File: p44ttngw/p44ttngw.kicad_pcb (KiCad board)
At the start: 2 copper layers, 90.5 x 56 mm, 67 parts, among them J1 CONN_02X04, J2 HLJ-6115ANL, J3 CONN_02X12, J4 USB_A, J6 USB_Micro_AB, J8 HLJ-6115ANL, P1 FDI_Cable, P3 CONN_02X02, SW1 Omron PB, U1 ONION-OMEGA2S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

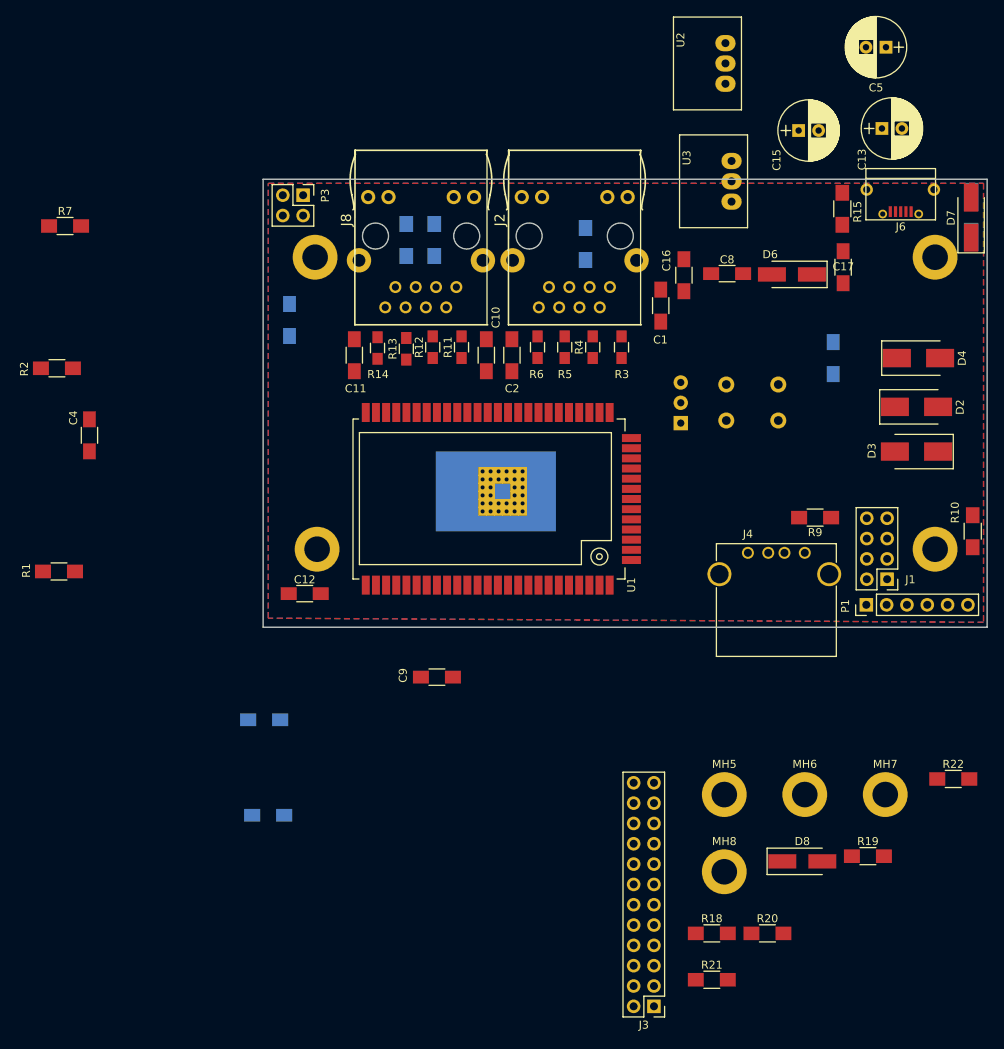
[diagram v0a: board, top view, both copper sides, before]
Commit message: Complete PCB for P44-DSB Hammond case, but mechanical check pending
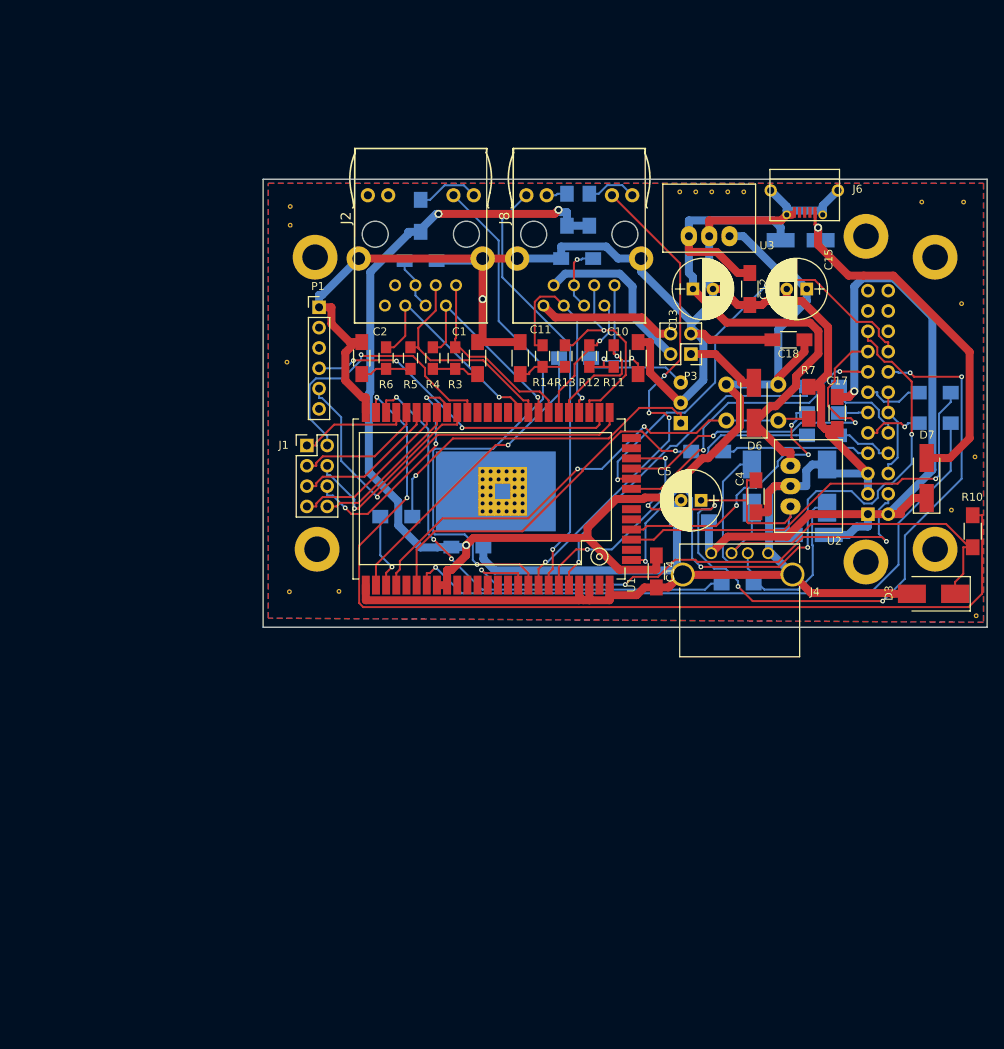
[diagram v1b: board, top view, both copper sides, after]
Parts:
- removed C19: 100nF, Capacitors_SMD:C_1206_HandSoldering
- removed MH5, MH6, MH7, MH8: CONN_01X01, Mounting_Holes:MountingHole_3.2mm_M3_DIN965_Pad
- added VIA: Stitching-VIA-0.6mm, plan44:Stitching-VIA-0.6mm, F.Cu at (124.1, 65.6)
- added VIA: Stitching-VIA-0.6mm, plan44:Stitching-VIA-0.6mm, F.Cu at (158.0, 105.4)
- added VIA: Stitching-VIA-0.6mm, plan44:Stitching-VIA-0.6mm, F.Cu at (161.1, 118.6)
- added VIA: Stitching-VIA-0.6mm, plan44:Stitching-VIA-0.6mm, F.Cu at (81.5, 115.5)
- added VIA: Stitching-VIA-0.6mm, plan44:Stitching-VIA-0.6mm, F.Cu at (75.3, 115.6)
- added VIA: Stitching-VIA-0.6mm, plan44:Stitching-VIA-0.6mm, F.Cu at (75.0, 86.9)
- added VIA: Stitching-VIA-0.6mm, plan44:Stitching-VIA-0.6mm, F.Cu at (75.4, 69.7)
- added VIA: Stitching-VIA-0.6mm, plan44:Stitching-VIA-0.6mm, F.Cu at (75.4, 67.4)
- added VIA: Stitching-VIA-0.6mm, plan44:Stitching-VIA-0.6mm, F.Cu at (126.1, 65.6)
- added VIA: Stitching-VIA-0.6mm, plan44:Stitching-VIA-0.6mm, F.Cu at (128.1, 65.6)
- added VIA: Stitching-VIA-0.6mm, plan44:Stitching-VIA-0.6mm, F.Cu at (130.1, 65.6)
- added VIA: Stitching-VIA-0.6mm, plan44:Stitching-VIA-0.6mm, F.Cu at (132.1, 65.6)
- added VIA: Stitching-VIA-0.6mm, plan44:Stitching-VIA-0.6mm, F.Cu at (154.3, 66.9)
- added VIA: Stitching-VIA-0.6mm, plan44:Stitching-VIA-0.6mm, F.Cu at (159.6, 66.9)
- added VIA: Stitching-VIA-0.6mm, plan44:Stitching-VIA-0.6mm, F.Cu at (159.3, 79.6)
- added VIA: Stitching-VIA-0.6mm, plan44:Stitching-VIA-0.6mm, F.Cu at (161.0, 98.7)
- C14, C18: moved to F.Cu
- C16, C8, C9, D2, D4, D8, R1, R15, R18, R19, R2, R20, R21, R22, R9: moved to B.Cu
- J3: value CONN_02X12 -> RAK831; footprint Pin_Headers:Pin_Header_Straight_2x12_Pitch2.54mm -> RAK831; moved to B.Cu
- moved R7 95.6 mm to (140.2, 91.9), turned to 270 degrees
- moved C4 83.7 mm to (133.6, 103.6)
- moved C18 80.9 mm to (137.7, 84.1), turned to 180 degrees
- moved P1 77.9 mm to (79.0, 80.0), turned to 0 degrees
- moved J1 74.4 mm to (77.5, 97.3), turned to 0 degrees
- moved R21 72.2 mm to (142.0, 93.2), turned to 180 degrees
- moved R1 69.8 mm to (111.0, 86.4), turned to 0 degrees
- moved R20 68.7 mm to (142.0, 89.9)
- moved C12 67.4 mm to (132.8, 77.7), turned to 270 degrees
- moved R18 63.8 mm to (142.0, 96.0)
- moved C5 61.2 mm to (126.7, 104.1)
- moved J3 61.1 mm to (147.3, 112.3)
- moved U2 58.5 mm to (137.9, 104.9), turned to 90 degrees
- moved C14 57.3 mm to (121.2, 113.0), turned to 270 degrees
- moved C3 56.3 mm to (125.7, 106.7), turned to 180 degrees
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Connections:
- net Net-(C4-Pad1) renamed /5VPWR
- C17 pad 1: +3V3 -> +5V
- C3 pad 1: +3V3 -> +5V
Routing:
- net GND: track 0.00 -> 363.1 mm, vias 0 -> 1
- net +3V3: track 0.00 -> 181.8 mm, vias 0 -> 3
- net /USB-: track 0.00 -> 121.5 mm, vias 0 -> 2
- net +5V: track 0.00 -> 95.8 mm, vias 0 -> 1
- net /SPI_MOSI: track 0.00 -> 94.7 mm, vias 0 -> 7
- net /RADIO_EN_B: track 0.00 -> 84.0 mm, vias 0 -> 1
- net /RAK_RESET: track 0.00 -> 80.0 mm, vias 0 -> 4
- net +24V: track 0.00 -> 73.8 mm
- net /ETH1_LED: track 0.00 -> 73.6 mm, vias 0 -> 1
- net /LNA_EN_A: track 0.00 -> 67.6 mm, vias 0 -> 3
- net /ETH0_LED: track 0.00 -> 63.0 mm, vias 0 -> 4
- net Net-(R7-Pad2): track 0.00 -> 62.3 mm, vias 0 -> 2
- net /USB+: track 0.00 -> 61.7 mm, vias 0 -> 3
- net /SPI_CLK: track 0.00 -> 55.5 mm, vias 0 -> 2
- net /WLAN_LED: track 0.00 -> 54.6 mm, vias 0 -> 1
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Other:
- net class PowerSmall: clearance 0.15 -> 0.1

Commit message: Completely redesigned for IP65 Hammond 1554E (90x90x60)
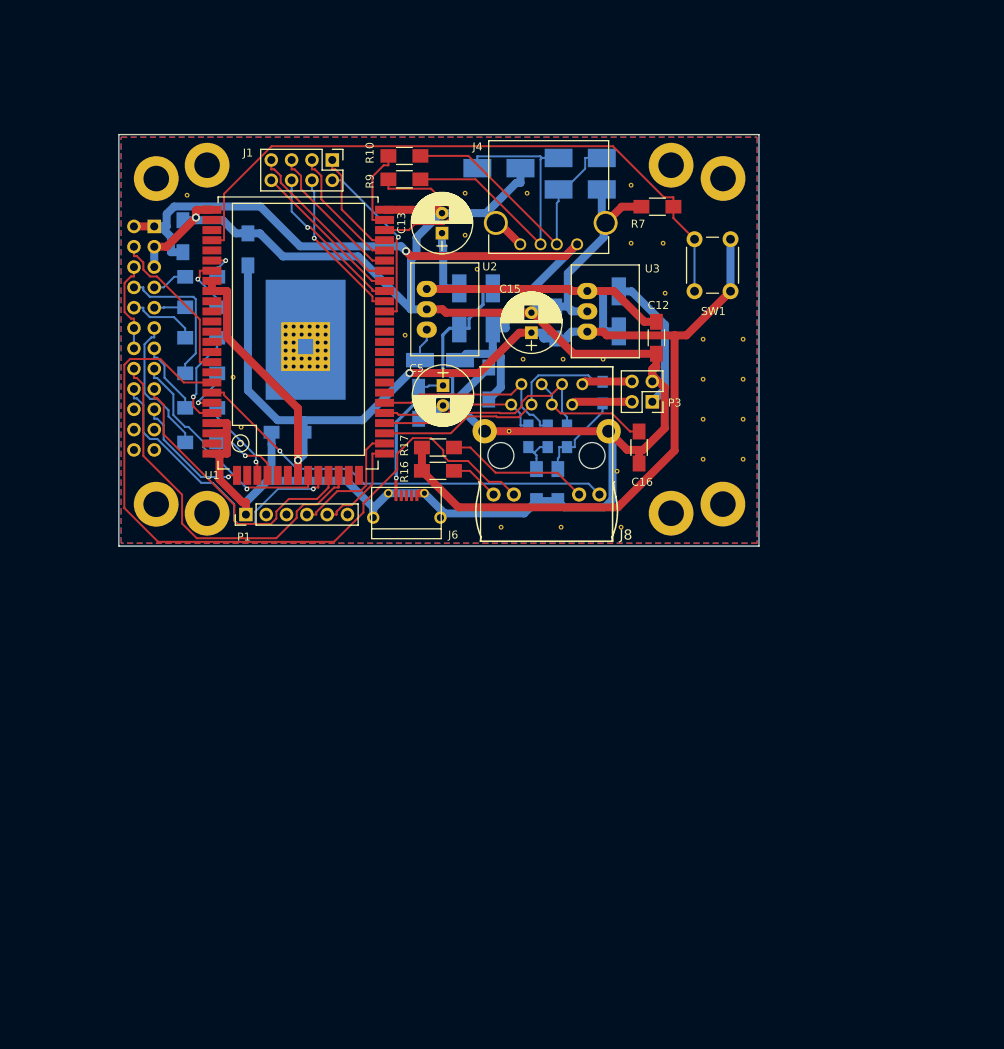
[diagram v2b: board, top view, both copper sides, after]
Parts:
- removed C1, C2: 100nF, Capacitors_SMD:C_1206_HandSoldering
- removed C8: 1uF, Capacitors_SMD:C_1206_HandSoldering
- removed D1: Everlight 339-1SURSYGW/S530-A3, LEDs:LED_D5.0mm-3
- removed J2: HLJ-6115ANL, plan44:HLJ-6115ANL
- removed R1: 470, Resistors_SMD:R_1206_HandSoldering
- removed R2: 1k2, Resistors_SMD:R_1206_HandSoldering
- removed R3, R4, R5, R6: 49.9_1%, Resistors_SMD:R_0805_HandSoldering
- removed R8: 1k, Resistors_SMD:R_1206_HandSoldering
- removed the VIA at (124.1, 65.6)
- removed the VIA at (158.0, 105.4)
- removed the VIA at (161.1, 118.6)
- removed the VIA at (81.5, 115.5)
- removed the VIA at (75.3, 115.6)
- removed the VIA at (75.0, 86.9)
- removed the VIA at (75.4, 69.7)
- removed the VIA at (75.4, 67.4)
- removed the VIA at (126.1, 65.6)
- removed the VIA at (128.1, 65.6)
- removed the VIA at (130.1, 65.6)
- removed the VIA at (132.1, 65.6)
- removed the VIA at (154.3, 66.9)
- removed the VIA at (159.6, 66.9)
- removed the VIA at (159.3, 79.6)
- removed the VIA at (161.0, 98.7)
- added VIA: Stitching-VIA-0.6mm, plan44:Stitching-VIA-0.6mm, F.Cu at (69.2, 95.0)
- added VIA: Stitching-VIA-0.6mm, plan44:Stitching-VIA-0.6mm, F.Cu at (118.0, 72.0)
- added VIA: Stitching-VIA-0.6mm, plan44:Stitching-VIA-0.6mm, F.Cu at (118.0, 64.8)
- added VIA: Stitching-VIA-0.6mm, plan44:Stitching-VIA-0.6mm, F.Cu at (105.0, 65.8)
- added VIA: Stitching-VIA-0.6mm, plan44:Stitching-VIA-0.6mm, F.Cu at (114.5, 86.5)
- added VIA: Stitching-VIA-0.6mm, plan44:Stitching-VIA-0.6mm, F.Cu at (109.5, 86.5)
- added VIA: Stitching-VIA-0.6mm, plan44:Stitching-VIA-0.6mm, F.Cu at (104.5, 86.5)
- added VIA: Stitching-VIA-0.6mm, plan44:Stitching-VIA-0.6mm, F.Cu at (132.0, 84.0)
- added VIA: Stitching-VIA-0.6mm, plan44:Stitching-VIA-0.6mm, F.Cu at (127.0, 84.0)
- added VIA: Stitching-VIA-0.6mm, plan44:Stitching-VIA-0.6mm, F.Cu at (132.0, 89.0)
- added VIA: Stitching-VIA-0.6mm, plan44:Stitching-VIA-0.6mm, F.Cu at (127.0, 89.0)
- added VIA: Stitching-VIA-0.6mm, plan44:Stitching-VIA-0.6mm, F.Cu at (116.2, 100.5)
- added VIA: Stitching-VIA-0.6mm, plan44:Stitching-VIA-0.6mm, F.Cu at (132.0, 94.0)
- added VIA: Stitching-VIA-0.6mm, plan44:Stitching-VIA-0.6mm, F.Cu at (127.0, 94.0)
- added VIA: Stitching-VIA-0.6mm, plan44:Stitching-VIA-0.6mm, F.Cu at (132.0, 99.0)
- added VIA: Stitching-VIA-0.6mm, plan44:Stitching-VIA-0.6mm, F.Cu at (127.0, 99.0)
- added VIA: Stitching-VIA-0.6mm, plan44:Stitching-VIA-0.6mm, F.Cu at (116.8, 107.5)
- added VIA: Stitching-VIA-0.6mm, plan44:Stitching-VIA-0.6mm, F.Cu at (109.2, 107.5)
- added VIA: Stitching-VIA-0.6mm, plan44:Stitching-VIA-0.6mm, F.Cu at (101.8, 107.5)
- added VIA: Stitching-VIA-0.6mm, plan44:Stitching-VIA-0.6mm, F.Cu at (68.2, 88.8)
- added VIA: Stitching-VIA-0.6mm, plan44:Stitching-VIA-0.6mm, F.Cu at (62.5, 66.0)
- added VIA: Stitching-VIA-0.6mm, plan44:Stitching-VIA-0.6mm, F.Cu at (102.8, 95.5)
- added VIA: Stitching-VIA-0.6mm, plan44:Stitching-VIA-0.6mm, F.Cu at (89.8, 83.5)
- added VIA: Stitching-VIA-0.6mm, plan44:Stitching-VIA-0.6mm, F.Cu at (98.8, 75.2)
- added VIA: Stitching-VIA-0.6mm, plan44:Stitching-VIA-0.6mm, F.Cu at (97.2, 71.0)
- added VIA: Stitching-VIA-0.6mm, plan44:Stitching-VIA-0.6mm, F.Cu at (97.2, 65.8)
- added VIA: Stitching-VIA-0.6mm, plan44:Stitching-VIA-0.6mm, F.Cu at (122.2, 78.2)
- added VIA: Stitching-VIA-0.6mm, plan44:Stitching-VIA-0.6mm, F.Cu at (122.0, 72.0)
- C10, C11, C14, C17, C18, C4, D3, D6, D7, R11, R12, R13, R14: moved to B.Cu
- C16, R16, R17, R9, SW1: moved to F.Cu
- J3: footprint RAK831 -> plan44:RAK831
- moved J3 101.2 mm to (58.7, 63.5), turned to 0 degrees
- moved R19 92.8 mm to (64.3, 80.0)
- moved R22 91.7 mm to (64.3, 92.6)
- moved R10 85.1 mm to (89.7, 61.1), turned to 0 degrees
- moved R18 78.1 mm to (64.3, 88.3), turned to 180 degrees
- moved R20 78.0 mm to (64.3, 83.8), turned to 180 degrees
- moved R21 77.8 mm to (64.3, 96.9), turned to 0 degrees
- moved C3 73.0 mm to (62.0, 71.1), turned to 90 degrees
- moved D3 67.1 mm to (111.6, 65.3), turned to 0 degrees
- moved R15 66.9 mm to (64.3, 76.2), turned to 0 degrees
- moved R9 65.5 mm to (89.7, 64.0)
- moved C14 65.0 mm to (70.1, 72.8), turned to 90 degrees
- moved J6 62.7 mm to (89.9, 104.9), turned to 0 degrees
- moved D7 58.2 mm to (100.7, 80.1)
- moved D4 57.1 mm to (101.5, 62.6), turned to 0 degrees
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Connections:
- U1 pad B10: /ETH1_RX- -> (no net)
- U1 pad B7: /ETH1_TX+ -> (no net)
- U1 pad B8: /ETH1_TX- -> (no net)
- U1 pad B9: /ETH1_RX+ -> (no net)
- U1 pad C23: Net-(R2-Pad1) -> (no net)
- U1 pad C24: Net-(R1-Pad1) -> (no net)
- U1 pad C9: /ETH1_LED -> (no net)
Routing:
- net /USB-: track 121.5 -> 10.7 mm, vias 2 -> 0
- net /RADIO_EN_B: track 84.0 -> 7.24 mm
- net /ETH1_LED: track 73.6 -> 0.00 mm, vias 1 -> 0
- net GND: track 363.1 -> 292.5 mm
- net /RAK_RESET: track 80.0 -> 15.7 mm, vias 4 -> 1
- net /SPI_MOSI: track 94.7 -> 47.0 mm, vias 7 -> 0
- net /LNA_EN_A: track 67.6 -> 20.1 mm, vias 3 -> 0
- net Net-(D1-Pad1): track 43.4 -> 0.00 mm, vias 1 -> 0
- net /RADIO_RST: track 52.7 -> 10.5 mm
- net /RADIO_EN_A: track 46.0 -> 4.32 mm
- net /USB+: track 61.7 -> 20.1 mm, vias 3 -> 0
- net Net-(R1-Pad1): track 38.8 -> 0.00 mm, vias 1 -> 0
- net /Omega_TX: track 51.3 -> 12.8 mm, vias 1 -> 0
- net /PA_G8: track 40.5 -> 6.37 mm
- net /PA_G16: track 43.5 -> 12.5 mm
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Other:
- board size 90.5 x 56 mm -> 80 x 51.4 mm

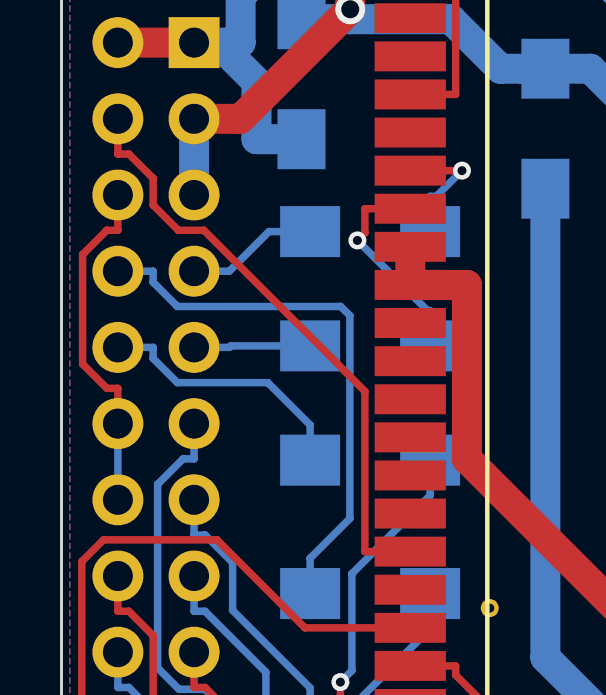
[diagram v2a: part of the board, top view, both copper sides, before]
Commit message: RAK831 pins 6,12 and 14 were connected together, but not to GND as they should. Fixed manually in layout, track width between 6 and 12 is narrow, no room for power net (and not needed).
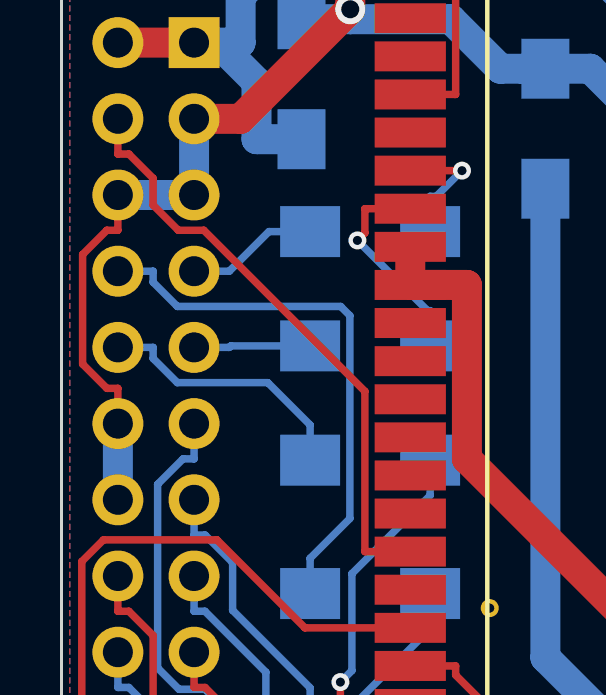
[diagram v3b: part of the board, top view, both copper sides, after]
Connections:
- J3 pad 12: Net-(J3-Pad12) -> GND
- J3 pad 14: Net-(J3-Pad12) -> GND
- J3 pad 20: (no net) -> Net-(J3-Pad20)
- J3 pad 21: (no net) -> Net-(J3-Pad21)
- J3 pad 22: (no net) -> Net-(J3-Pad22)
- J3 pad 23: (no net) -> Net-(J3-Pad23)
- J3 pad 24: (no net) -> Net-(J3-Pad24)
- J3 pad 6: Net-(J3-Pad12) -> GND
- J6 pad 2: (no net) -> Net-(J6-Pad2)
- J6 pad 3: (no net) -> Net-(J6-Pad3)
- J6 pad 4: (no net) -> Net-(J6-Pad4)
- MH1 pad 1: (no net) -> Net-(MH1-Pad1)
- MH2 pad 1: (no net) -> Net-(MH2-Pad1)
- MH3 pad 1: (no net) -> Net-(MH3-Pad1)
- MH4 pad 1: (no net) -> Net-(MH4-Pad1)
- P1 pad 2: (no net) -> Net-(P1-Pad2)
- P1 pad 3: (no net) -> Net-(P1-Pad3)
- P1 pad 6: (no net) -> Net-(P1-Pad6)
- U1 pad A12: (no net) -> Net-(U1-PadA12)
- U1 pad A13: (no net) -> Net-(U1-PadA13)
- U1 pad A2: (no net) -> Net-(U1-PadA2)
- U1 pad A5: (no net) -> Net-(U1-PadA5)
- U1 pad A6: (no net) -> Net-(U1-PadA6)
- U1 pad B10: (no net) -> Net-(U1-PadB10)
- U1 pad B11: (no net) -> Net-(U1-PadB11)
- U1 pad B12: (no net) -> Net-(U1-PadB12)
- U1 pad B13: (no net) -> Net-(U1-PadB13)
- U1 pad B14: (no net) -> Net-(U1-PadB14)
- U1 pad B7: (no net) -> Net-(U1-PadB7)
- U1 pad B8: (no net) -> Net-(U1-PadB8)
- U1 pad B9: (no net) -> Net-(U1-PadB9)
- U1 pad C11: (no net) -> Net-(U1-PadC11)
- U1 pad C12: (no net) -> Net-(U1-PadC12)
- U1 pad C13: (no net) -> Net-(U1-PadC13)
- U1 pad C14: (no net) -> Net-(U1-PadC14)
- U1 pad C15: (no net) -> Net-(U1-PadC15)
- U1 pad C16: (no net) -> Net-(U1-PadC16)
- U1 pad C2: (no net) -> Net-(U1-PadC2)
- U1 pad C21: (no net) -> Net-(U1-PadC21)
- U1 pad C23: (no net) -> Net-(U1-PadC23)
- U1 pad C24: (no net) -> Net-(U1-PadC24)
- U1 pad C9: (no net) -> Net-(U1-PadC9)
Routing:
- net GND: track 292.5 -> 306.6 mm
- net Net-(J3-Pad12): track 11.6 -> 0.00 mm
